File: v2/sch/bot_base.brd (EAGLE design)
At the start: 120.3 x 93 mm, 35 parts, among them K1 SKQGADE010, Q0 QWIIC_RIGHT_ANGLE, U1 ESP32-C3-MINI-1-N4, U2 AP7370-33SA (or MCP1703T-3302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, U4 LGS4084HB5

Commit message: routing almost finished
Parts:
- removed JUMPER_LIPO_CHG: NO-FIT, solder_jumper:WIRELINK2
- removed K1: SKQGADE010, Seeed-OPL-Button:SW4-SMD-5.2X5.2X1.5MM
- added K2: DTSM-62K-S-V-T/R, Seeed-OPL-Button:SW4-SMD-6.0X6.0X5.0MM
- added R10: 10k, rcl:R0603
- added SERVO: (no value), pinhead-2:1X03-S
- moved BAT 37.1 mm to (57.0, 11.0)
- moved C2 34.7 mm to (103.0, 44.0)
- moved C1 25.7 mm to (99.0, 41.0), turned to 270 degrees
- moved Q0 24.9 mm to (112.2, 62.9), turned to 90 degrees
- moved LED1 21.3 mm to (74.6, 9.40), turned to 270 degrees
- moved U2 19.0 mm to (103.0, 41.0), turned to 270 degrees
- moved U4 18.1 mm to (78.6, 8.40)
- moved R2 15.9 mm to (74.8, 10.8), turned to 180 degrees
- moved R1 11.7 mm to (82.4, 8.40), turned to 90 degrees
- moved R8 9.40 mm to (23.0, 28.6), turned to 270 degrees
- moved C3 6.81 mm to (72.4, 68.8), turned to 180 degrees
- moved R7 3.10 mm to (73.0, 72.8)
- moved R11 2.78 mm to (110.4, 58.4), turned to 90 degrees
- moved C4 1.65 mm to (71.4, 24.4)
- moved U$3 1.61 mm to (71.6, 20.8)
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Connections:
- removed net N$2: JUMPER_LIPO_CHG.P$1, U4.3
- removed net N$7: K1.1, U1.23
- new net BOOT: K2.1, U1.23
- new net MOTOR1A_LV: U$3.8, U1.18
- new net MOTOR1B_LV: U$3.5, U1.21
- new net MOTOR2A_LV: U$4.8, U1.20
- new net MOTOR2B_LV: U$4.5, U1.19
- net +5V: now also SERVO.2, U$9.P$1
- net BUTTONS: now also R10.2
- net GND: now also C3.1, C4.1, K2.2, SERVO.1, U$5.4; no longer K1.4
- net MOTOR1A: now also U$3.4, U$6.P$2; no longer U$3.8, U$6.P$1, U1.18
- net MOTOR1B: now also U$3.2, U$6.P$1; no longer U$3.5, U$6.P$2, U1.21
- net MOTOR2A: now also U$4.4, U$7.P$2; no longer U$4.8, U$7.P$1, U1.20
- net MOTOR2B: now also U$4.2, U$7.P$1; no longer U$4.5, U$7.P$2, U1.19
- net TXD0_GPIO21: now also SERVO.3
- net VBAT: now also U$5.1, U4.3; no longer JUMPER_LIPO_CHG.P$2
- net VCC: now also R10.1; no longer U$9.P$1
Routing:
- net +5V: track 0.00 -> 270.1 mm, vias 0 -> 1
- net GND: track 0.00 -> 210.6 mm
- net VCC: track 0.00 -> 172.9 mm, vias 0 -> 4
- net MOTOR1_SENS: track 0.00 -> 110.9 mm, vias 0 -> 1
- net MOTOR_LED: track 0.00 -> 110.2 mm, vias 0 -> 2
- net BUTTONS: track 0.00 -> 105.5 mm
- net TXD0_GPIO21: track 0.00 -> 105.2 mm, vias 0 -> 3
- net NEOPIXEL: track 0.00 -> 89.5 mm
- net VBAT: track 0.00 -> 85.0 mm
- net MOTOR2_SENS: track 0.00 -> 79.3 mm, vias 0 -> 1
- net USB_VBUS: track 0.00 -> 72.8 mm, vias 0 -> 2
- net MOTOR1A_LV: track 0.00 -> 64.7 mm, vias 0 -> 2
- net MOTOR1B_LV: track 0.00 -> 64.0 mm, vias 0 -> 2
- net USB_DN: track 0.00 -> 40.7 mm
- net USB_DP: track 0.00 -> 37.4 mm
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
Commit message: first protos sent off
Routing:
- net GND: track 210.6 -> 494.5 mm, vias 0 -> 31
- net VCC: track 172.9 -> 234.6 mm, vias 4 -> 6
- net MOTOR_LED: track 110.2 -> 127.7 mm
- net TXD0_GPIO21: track 105.2 -> 106.1 mm
- added copper zone on layer 1, net GND
- added copper zone on layer 16, net GND

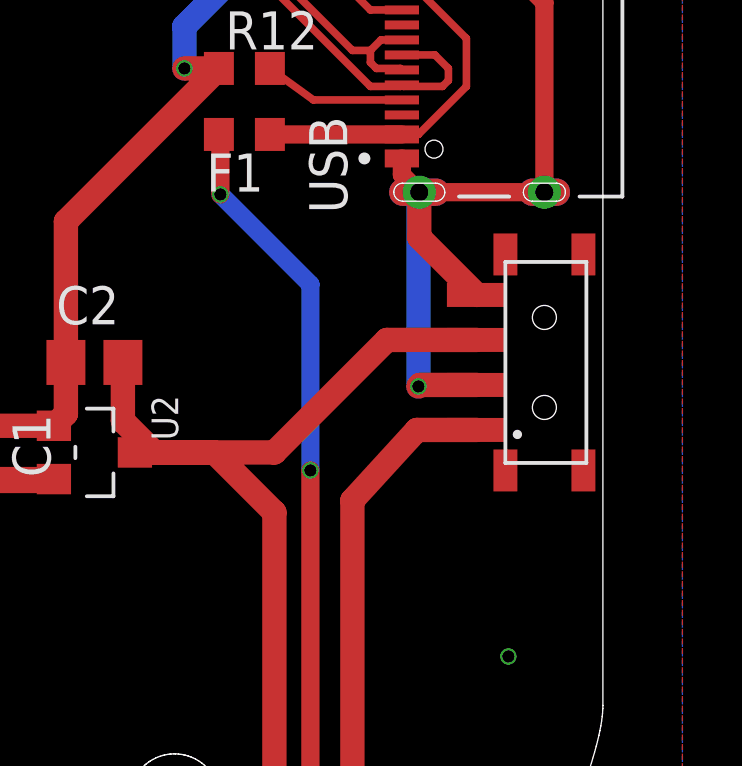
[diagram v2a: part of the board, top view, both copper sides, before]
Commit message: switch update
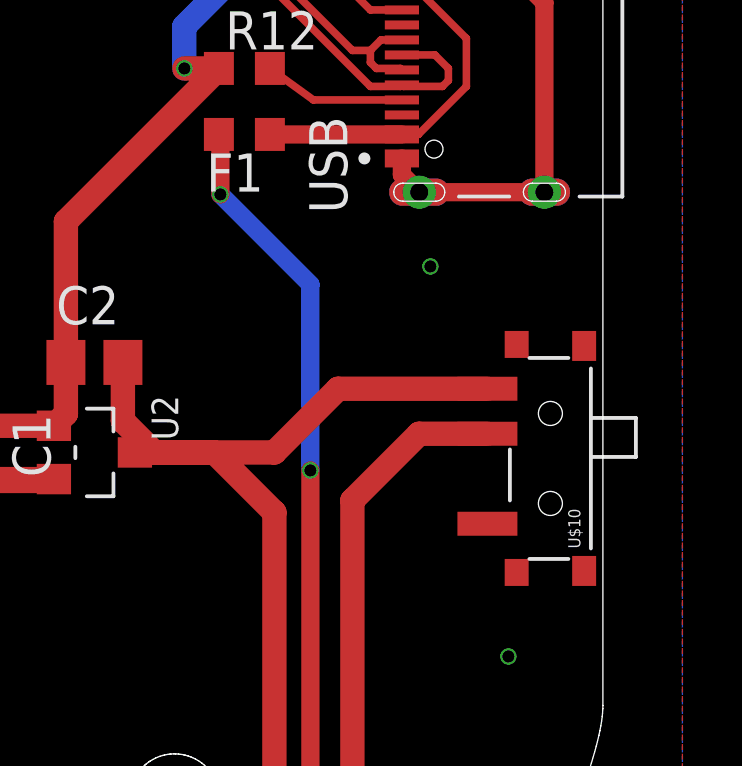
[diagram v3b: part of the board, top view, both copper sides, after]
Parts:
- removed U$5: LY-SK-03, pimoroni-mechanical:LY-SK-03
- added U$10: MSK-12C02_SMD_SPDT_SWITCH, switch-MSK-12C02:MSK-12C02
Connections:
- net +5V: now also U$10.L1; no longer U$5.3
- net GND: no longer U$5.2, U$5.4
- net VBAT: now also U$10.COM; no longer U$5.1
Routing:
- net GND: track 494.5 -> 481.8 mm
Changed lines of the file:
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@@
 <setting verticaltext="up"/>
 </settings>
-<grid distance="0.2" unitdist="mm" unit="mm" style="lines" multiple="1" display="no" altdistance="0.025" altunitdist="inch" altunit="inch"/>
+<grid distance="0.2" unitdist="mm" unit="mm" style="lines" multiple="1" display="yes" altdistance="0.025" altunitdist="inch" altunit="inch"/>
 <layers>
 <layer number="1" name="Top" color="4" fill="1" visible="yes" active="yes"/>
@@
 <element name="R12" library="rcl" package="R0603" value="5K1" x="108" y="53.8"/>
 <element name="F1" library="rcl" package="R0603" value="MF-FSMF050X-2" x="108" y="51.6" rot="R180"/>
-<element name="U$5" library="pimoroni-mechanical" package="LY-SK-03" value="LY-SK-03" x="118" y="44" rot="R90"/>
 <element name="LED2" library="led" package="CHIPLED_0603" value="RED" x="76" y="75" rot="R270"/>
 <element name="R3" library="rcl" package="R0603" value="1K" x="73" y="75"/>
@@
 <attribute name="MPN" value="DTSM-62K-S-V-T/R" x="71.6" y="82" size="1.778" layer="27" rot="R180" display="off"/>
 </element>
+<element name="U$10" library="switch-MSK-12C02" package="MSK-12C02" value="MSK-12C02_SMD_SPDT_SWITCH" x="118.2" y="40.8" rot="R90"/>
 </elements>
 <signals>
@@
 <contactref element="R12" pad="1"/>
 <contactref element="R11" pad="2"/>
-<contactref element="U$5" pad="2"/>
 <contactref element="Q0" pad="1"/>
 <contactref element="U$9" pad="P$2"/>
 <contactref element="C4" pad="1"/>
 <contactref element="C3" pad="1"/>
-<contactref element="U$5" pad="4"/>
 <wire x1="101.65" y1="41.889" x2="99.061" y2="41.889" width="0.8128" layer="1"/>
 <wire x1="99.061" y1="41.889" x2="99" y2="41.95" width="0.8128" layer="1"/>
@@
 <via x="99" y="43.6" extent="1-16" drill="0.4"/>
 <wire x1="99" y1="43.6" x2="99" y2="41.95" width="0.8128" layer="1"/>
-<wire x1="113.83" y1="49.675" x2="113.83" y2="48.17" width="0.8128" layer="1"/>
-<wire x1="113.83" y1="48.17" x2="115.75" y2="46.25" width="0.8128" layer="1"/>
-<wire x1="115.75" y1="43.25" x2="113.85" y2="43.25" width="0.8128" layer="1"/>
-<wire x1="113.85" y1="43.25" x2="113.8" y2="43.2" width="0.8128" layer="1"/>
-<via x="113.8" y="43.2" extent="1-16" drill="0.4"/>
-<wire x1="113.8" y1="43.2" x2="113.8" y2="49.645" width="0.8128" layer="16"/>
+<via x="114.2" y="47.2" extent="1-16" drill="0.4"/>
 <wire x1="113.8" y1="49.645" x2="113.83" y2="49.675" width="0.8128" layer="16"/>
 <wire x1="77.294" y1="8.4" x2="72.8" y2="8.4" width="0.4064" layer="1"/>
@@
 <signal name="VBAT">
 <contactref element="BAT" pad="2"/>
-<contactref element="U$5" pad="1"/>
-<wire x1="115.75" y1="41.75" x2="113.75" y2="41.75" width="0.8128" layer="1"/>
-<wire x1="113.75" y1="41.75" x2="111.6" y2="39.4" width="0.8128" layer="1"/>
 <wire x1="111.6" y1="39.4" x2="111.6" y2="24.4" width="0.8128" layer="1"/>
 <wire x1="111.6" y1="24.4" x2="92.6" y2="5.6" width="0.8128" layer="1"/>
@@
 <wire x1="77.294" y1="7.45" x2="77.094" y2="5.706" width="0.6096" layer="1"/>
 <wire x1="77.094" y1="5.706" x2="77.2" y2="5.6" width="0.6096" layer="1"/>
+<contactref element="U$10" pad="COM"/>
+<wire x1="116.1" y1="41.623" x2="113.823" y2="41.623" width="0.8128" layer="1"/>
+<wire x1="113.823" y1="41.623" x2="111.6" y2="39.4" width="0.8128" layer="1"/>
 </signal>
 <signal name="N$18">
@@
 <contactref element="C3" pad="2"/>
 <contactref element="U$4" pad="1"/>
-<contactref element="U$5" pad="3"/>
-<wire x1="115.75" y1="44.75" x2="112.75" y2="44.75" width="0.8128" layer="1"/>
-<wire x1="112.75" y1="44.75" x2="109" y2="41" width="0.8128" layer="1"/>
 <wire x1="109" y1="41" x2="105" y2="41" width="0.8128" layer="1"/>
 <wire x1="105" y1="41" x2="104.35" y2="41" width="0.8128" layer="1"/>
@@
 <wire x1="29" y1="44.8" x2="29" y2="28.2" width="0.8128" layer="16"/>
 <wire x1="29" y1="28.2" x2="28.9" y2="28.1" width="0.8128" layer="16"/>
+<contactref element="U$10" pad="L1"/>
+<wire x1="116.1" y1="43.123" x2="111.123" y2="43.123" width="0.8128" layer="1"/>
+<wire x1="111.123" y1="43.123" x2="109" y2="41" width="0.8128" layer="1"/>
 </signal>
 <signal name="USB_DP">

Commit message: mid-update, fixing issues
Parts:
- added LED3: RED, led:CHIPLED_0603
- added R13: 10k, rcl:R0603
- R4, R5: value 300 -> 100
- U$1, U$2: value XL-ITR9608 -> XL-ITR9707; device ir-XINGLIGHT-XL-ITR9608:XL-ITR9608 -> ir-XINGLIGHT-XL-ITR9608:XL-ITR9707
- moved BAT 20.0 mm to (57.0, 31.0)
- moved C1 16.4 mm to (112.0, 31.0)
- moved C2 16.4 mm to (116.0, 34.0)
- moved U2 16.4 mm to (116.0, 31.0)
- moved R1 12.0 mm to (71.6, 13.6), turned to 270 degrees
- moved LED1 6.00 mm to (68.6, 9.40)
- moved R2 6.00 mm to (68.8, 10.8)
- moved U4 6.00 mm to (72.6, 8.40)
- moved SERVO 5.00 mm to (31.8, 46.6)
- moved R6 1.50 mm to (24.5, 24.1)
- moved R8 1.50 mm to (24.5, 28.6)
- moved R9 1.50 mm to (24.5, 69.0)
- moved U$1 1.50 mm to (19.3, 30.4)
- moved U$2 1.50 mm to (19.3, 62.7)
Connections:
- new net N$2: LED3.C, R13.2
- net +5V: now also U$9.P$3, U$9.P$4
- net BUTTONS: now also U$8.P$3, U$8.P$4
- net GND: now also R13.1, U$9.P$5, U$9.P$6
- net MOTOR1A: now also U$6.P$5, U$6.P$6
- net MOTOR1B: now also U$6.P$3, U$6.P$4
- net MOTOR2A: now also U$7.P$5, U$7.P$6
- net MOTOR2B: now also U$7.P$3, U$7.P$4
- net N$3: now also U$1.P$1; no longer U$1.P$2
- net N$5: now also U$2.P$1; no longer U$2.P$2
- net NEOPIXEL: now also U$8.P$5, U$8.P$6
- net VCC: now also LED3.A, U$1.P$2, U$2.P$2; no longer U$1.P$1, U$2.P$1
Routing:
- net GND: track 481.8 -> 374.8 mm, vias 31 -> 29
- net VBAT: track 85.3 -> 2.28 mm
- net +5V: track 269.8 -> 193.4 mm
- net USB_VBUS: track 72.8 -> 8.99 mm
- net VCC: track 234.6 -> 221.5 mm
- net TXD0_GPIO21: track 106.1 -> 101.1 mm
- net N$5: track 27.4 -> 24.7 mm
- net N$18: track 2.54 -> 0.00 mm
- net MOTOR_LED: track 127.7 -> 126.2 mm
- net N$3: track 23.2 -> 21.7 mm
- net NEOPIXEL: track 89.5 -> 88.2 mm
- net MOTOR1_SENS: track 110.9 -> 109.8 mm
- net MOTOR2_SENS: track 79.3 -> 78.2 mm
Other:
- outline, holes or cut-outs redrawn

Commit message: latest relayout
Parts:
- removed U2: AP7370-33SA (or MCP1703T-3302E/CB backup), mcp1703t:SOT23A
- added C5: 4.7uF, rcl:C0805
- added U$5: AP7361C-33E-13, vreg:SOT223
- moved C2 64.1 mm to (52.5, 25.5)
- moved C1 54.7 mm to (58.5, 42.5), turned to 0 degrees
- moved U1 48.8 mm to (46.0, 60.0), turned to 0 degrees
- moved R3 38.3 mm to (49.1, 45.1), turned to 90 degrees
- moved LED2 38.2 mm to (49.0, 48.0), turned to 0 degrees
- moved R7 36.0 mm to (47.0, 47.9), turned to 270 degrees
- moved U4 35.8 mm to (42.6, 27.9)
- moved R1 34.3 mm to (42.4, 31.6), turned to 0 degrees
- moved LED1 21.5 mm to (67.6, 30.9), turned to 0 degrees
- moved R4 18.7 mm to (24.5, 58.5)
- moved C3 17.6 mm to (56.9, 60.5), turned to 270 degrees
- moved R10 17.3 mm to (24.5, 60.6), turned to 0 degrees
- moved R2 16.9 mm to (67.5, 27.7), turned to 90 degrees
- moved U$3 16.4 mm to (60.8, 33.2), turned to 0 degrees
- moved R5 15.6 mm to (24.5, 26.1)
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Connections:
- net +5V: now also LED3.A, U$5.1; no longer C2.2, U2.3
- net GND: now also C5.1, U$5.2; no longer U2.1
- net VBAT: now also C2.2
- net VCC: now also C5.2, U$5.3; no longer LED3.A, U2.2
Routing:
- net GND: track 374.8 -> 520.2 mm, vias 29 -> 38
- net VBAT: track 2.28 -> 102.1 mm, vias 0 -> 2
- net USB_VBUS: track 8.99 -> 107.6 mm
- net +5V: track 193.4 -> 269.3 mm, vias 1 -> 6
- net MOTOR_LED: track 126.2 -> 51.1 mm
- net MOTOR1_SENS: track 109.8 -> 34.7 mm
- net MOTOR2_SENS: track 78.2 -> 32.8 mm, vias 1 -> 2
- net MOTOR1A_LV: track 64.7 -> 24.3 mm
- net MOTOR1B_LV: track 64.0 -> 24.0 mm
- net BUTTONS: track 105.5 -> 69.8 mm
- net VCC: track 221.5 -> 186.2 mm, vias 6 -> 4
- net RXD0_GPIO20: track 32.3 -> 65.1 mm
- net NEOPIXEL: track 88.2 -> 57.8 mm, vias 0 -> 1
- net BOOT: track 10.5 -> 40.9 mm
- net MOTOR1A: track 4.05 -> 32.7 mm
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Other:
- board text added: "OFF ON"

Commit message: update for most recent prototypes
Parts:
- added R14: 1K, rcl:R0603
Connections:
- net GND: now also R14.1
- net MOTOR2A_LV: now also R14.2
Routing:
- net MOTOR2A_LV: track 19.6 -> 25.8 mm
- net GND: track 520.2 -> 526.0 mm
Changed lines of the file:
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@@
 <element name="U$5" library="vreg" package="SOT223" value="AP7361C-33E-13" x="57.5" y="48.5"/>
 <element name="C5" library="rcl" package="C0805" value="4.7uF" x="35.6" y="54.8" rot="R90"/>
+<element name="R14" library="rcl" package="R0603" value="1K" x="44.4" y="47.4"/>
 </elements>
 <signals>
@@
 <via x="71.9" y="59.6" extent="1-16" drill="0.3"/>
 <via x="109.7" y="46.9" extent="1-16" drill="0.3"/>
+<contactref element="R14" pad="1"/>
+<wire x1="43.55" y1="47.4" x2="40.7" y2="47.4" width="0.254" layer="1"/>
+<wire x1="40.7" y1="47.4" x2="39" y2="45.7" width="0.254" layer="1"/>
+<wire x1="39" y1="45.7" x2="38.4" y2="45.7" width="0.254" layer="1"/>
+<wire x1="81.8" y1="86" x2="101.3" y2="85.9" width="0" layer="19" extent="1-1"/>
+<wire x1="70" y1="86.6" x2="81.8" y2="86" width="0" layer="19" extent="1-1"/>
+<wire x1="72.159" y1="78.471" x2="70" y2="86.6" width="0" layer="19" extent="1-1"/>
+<wire x1="64.6" y1="35.6" x2="61.435" y2="35.8162" width="0" layer="19" extent="1-1"/>
+<wire x1="109.7" y1="46.9" x2="112.7" y2="48.545" width="0" layer="19" extent="16-16"/>
+<wire x1="36.3" y1="61.4" x2="39.9" y2="61" width="0" layer="19" extent="1-1"/>
+<wire x1="61.9" y1="46.7" x2="57.5" y2="46.9" width="0" layer="19" extent="16-16"/>
+<wire x1="63.7" y1="42.1" x2="61.9" y2="46.7" width="0" layer="19" extent="1-1"/>
+<wire x1="117" y1="30" x2="116.6" y2="35.35" width="0" layer="19" extent="1-1"/>
+<wire x1="5.4" y1="8.3" x2="6.3" y2="14.8" width="0" layer="19" extent="16-16"/>
+<wire x1="29" y1="60.3" x2="27.9" y2="53.1" width="0" layer="19" extent="16-16"/>
+<wire x1="67.2" y1="53" x2="60.7" y2="56.5" width="0" layer="19" extent="1-1"/>
+<wire x1="71.7" y1="53.9" x2="67.2" y2="53" width="0" layer="19" extent="1-1"/>
+<wire x1="71.9" y1="59.6" x2="71.7" y2="53.9" width="0" layer="19" extent="1-1"/>
+<wire x1="113.7" y1="68.7" x2="112.2" y2="61.4" width="0" layer="19" extent="1-1"/>
+<wire x1="8.3" y1="61.4" x2="16.2" y2="59.7" width="0" layer="19" extent="16-16"/>
+<wire x1="0.9" y1="61.3" x2="8.3" y2="61.4" width="0" layer="19" extent="1-1"/>
+<wire x1="45.6" y1="7.7" x2="48.2" y2="17" width="0" layer="19" extent="1-1"/>
+<wire x1="65.6" y1="7.6" x2="55.1" y2="10.1" width="0" layer="19" extent="1-1"/>
+<wire x1="29.9" y1="7.9" x2="45.6" y2="7.7" width="0" layer="19" extent="1-1"/>
+<wire x1="101" y1="8.2" x2="78.4" y2="10.1" width="0" layer="19" extent="1-1"/>
 </signal>
 <signal name="MOTOR2_SENS">
@@
 <via x="47.6" y="53.3" extent="1-16" drill="0.3"/>
 <wire x1="47.6" y1="53.3" x2="47.6" y2="52.4" width="0.254" layer="1"/>
+<contactref element="R14" pad="2"/>
+<wire x1="47.6" y1="52.4" x2="47.6" y2="50.8" width="0.254" layer="1"/>
+<wire x1="47.6" y1="50.8" x2="47.2" y2="50.8" width="0.254" layer="1"/>
+<wire x1="47.2" y1="50.8" x2="45.5" y2="49.1" width="0.254" layer="1"/>
+<wire x1="45.5" y1="49.1" x2="45.5" y2="47.65" width="0.254" layer="1"/>
+<wire x1="45.5" y1="47.65" x2="45.25" y2="47.4" width="0.254" layer="1"/>
 </signal>
 <signal name="MOTOR1B_LV">
